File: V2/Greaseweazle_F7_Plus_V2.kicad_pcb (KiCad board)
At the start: 2 copper layers, 80 x 50 mm, 68 parts, among them J1 Wurth 694106301002, J10 PIN1X2, J11 PIN1X2, J12 IDC Box Header, J2 USB_B, J3 Molex 105017-1001, J4 TE EI 171826-4, J5 PIN1X3, J6 PIN1X2, J7 PIN1X5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

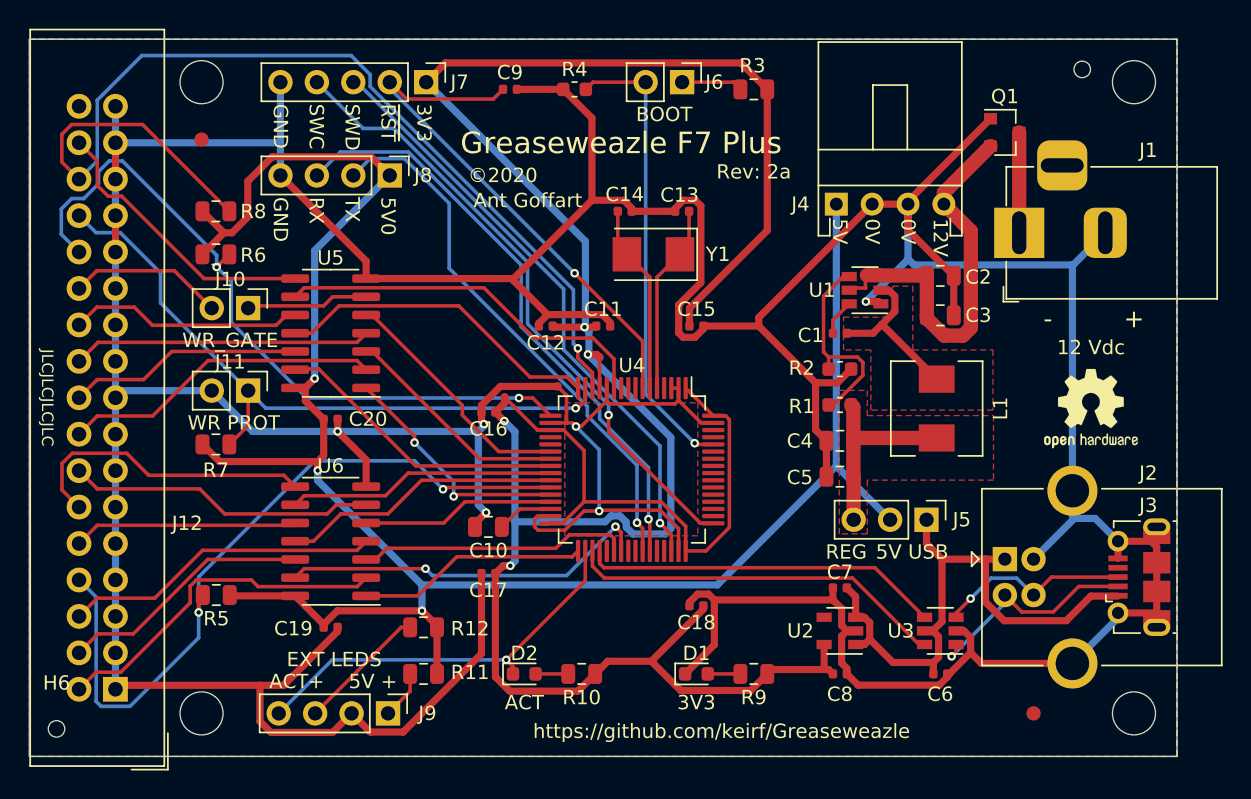
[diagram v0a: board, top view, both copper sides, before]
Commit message: added copper fill below mcu and L1 improved power connections of mcu
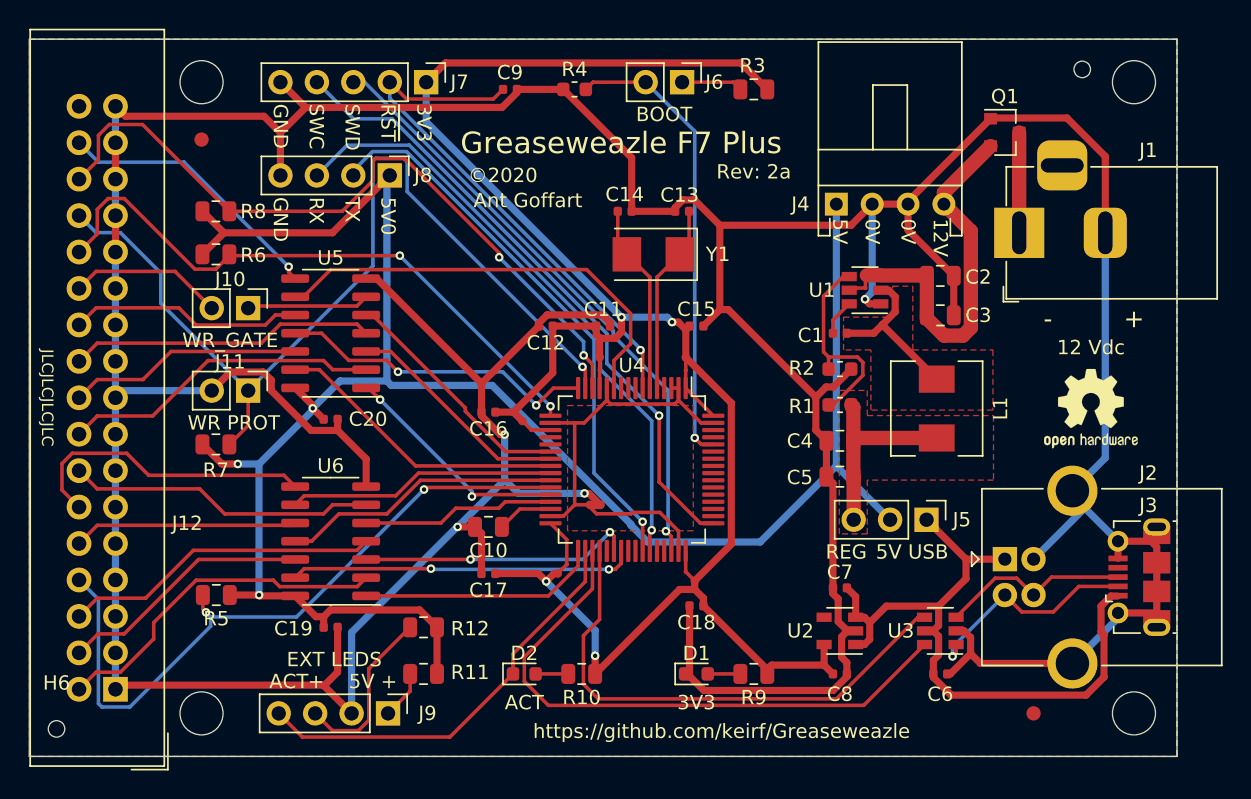
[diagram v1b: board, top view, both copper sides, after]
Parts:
- removed U10: NarrowPowerAdapter, greaseweazle:NarrowPowerAdapter_0.60_to_0.25
- added U11: NarrowPowerAdapter, greaseweazle:NarrowPowerAdapter_0.60_to_0.25, F.Cu at (186.8, 137.2)
- added U12: NarrowPowerAdapter, greaseweazle:NarrowPowerAdapter_0.60_to_0.25, F.Cu at (195.8, 122.2)
- added U13: NarrowPowerAdapter, greaseweazle:NarrowPowerAdapter_0.60_to_0.25, F.Cu at (196.4, 137.8)
- added U15: NarrowPowerAdapter, greaseweazle:NarrowPowerAdapter_0.60_to_0.25_thick, F.Cu at (189.8, 132.5)
- moved U7 3.56 mm to (189.8, 122.2), turned to 0 degrees
- moved U8 2.06 mm to (184.4, 126.6)
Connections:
- U4 pad 1: Net-(U4-Pad1) -> Net-(U12-Pad2)
- U4 pad 12: Net-(U4-Pad12) -> /GND_for_U4
- U4 pad 13: Net-(U10-Pad2) -> Net-(U4-Pad13)
- U4 pad 18: Net-(U4-Pad12) -> /GND_for_U4
- U4 pad 19: Net-(U4-Pad1) -> Net-(U4-Pad19)
- U4 pad 2: Net-(U4-Pad12) -> /GND_for_U4
- U4 pad 3: Net-(U4-Pad12) -> /GND_for_U4
- U4 pad 31: Net-(U4-Pad12) -> /GND_for_U4
- U4 pad 32: Net-(U4-Pad1) -> Net-(U11-Pad2)
- U4 pad 47: Net-(U4-Pad12) -> /GND_for_U4
- U4 pad 48: Net-(U4-Pad1) -> Net-(U13-Pad2)
- U4 pad 63: Net-(U4-Pad12) -> /GND_for_U4
- U4 pad 64: Net-(U4-Pad1) -> Net-(U12-Pad2)
- U7 pad 1: GND -> +3V3
- U7 pad 2: Net-(U4-Pad12) -> Net-(U4-Pad13)
- U8 pad 2: Net-(U4-Pad1) -> Net-(U4-Pad19)
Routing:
- net Net-(U4-Pad12): track 38.3 -> 0.00 mm, vias 2 -> 0
- net Net-(U4-Pad1): track 37.4 -> 0.00 mm
- net /GND_for_U4: track 0.00 -> 32.3 mm
- net +3V3: track 152.7 -> 126.6 mm
- net /~RD_DAT~: track 73.3 -> 51.6 mm, vias 1 -> 2
- net /~WR_PROT~: track 47.5 -> 65.5 mm
- net /USB_D-: track 26.5 -> 41.4 mm
- net /USB_D+: track 25.1 -> 36.3 mm
- net /~TRK_00~: track 50.2 -> 42.9 mm
- net /USB_VBUS: track 41.1 -> 47.2 mm
- net GND: track 381.9 -> 376.8 mm
- net /~SIDE~: track 26.6 -> 31.1 mm
- net Net-(U12-Pad2): track 0.00 -> 3.97 mm
- net Net-(U11-Pad2): track 0.00 -> 3.34 mm
- net /~INDEX~: track 52.6 -> 49.3 mm
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- added copper zone on F.Cu, net /GND_for_U4
- removed copper zone on F.Cu, net Net-(U4-Pad12)

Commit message: added via to get better copper fill made 5Vreg thicker
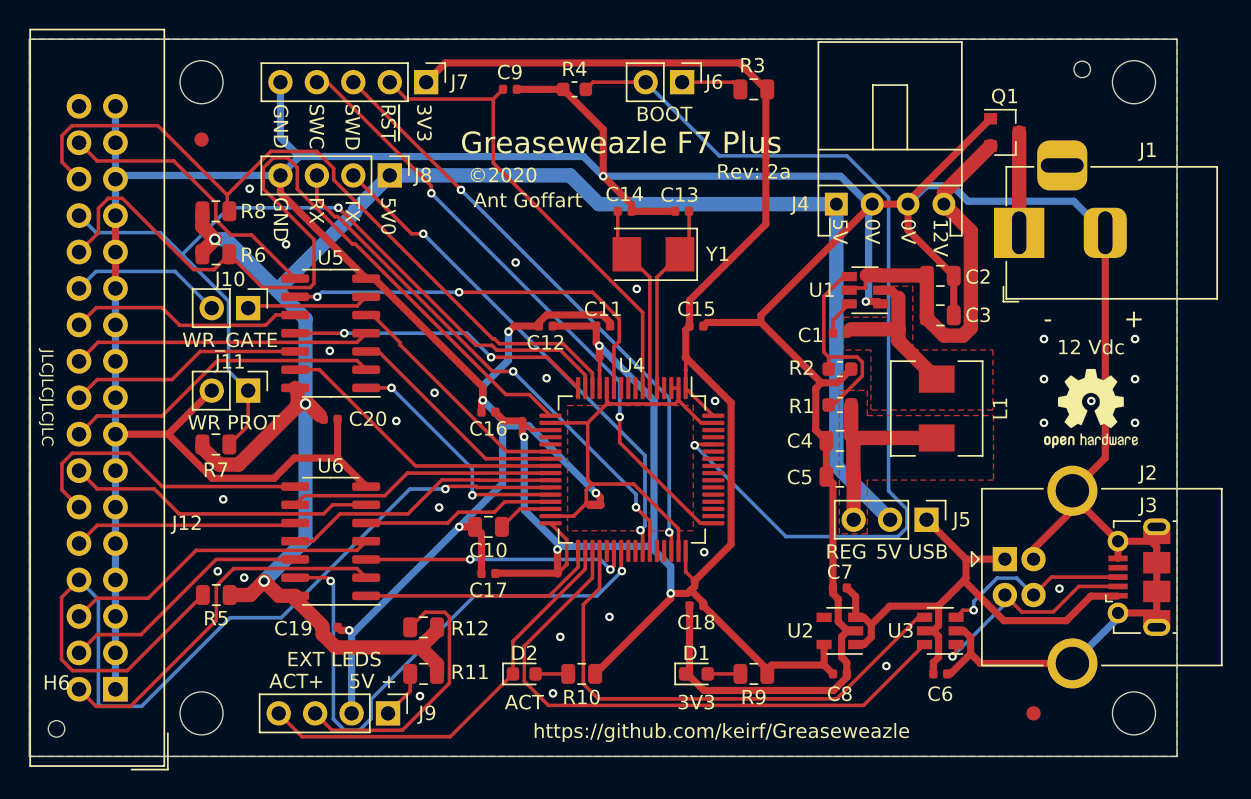
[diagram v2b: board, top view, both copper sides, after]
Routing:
- net /BOOT: track 32.1 -> 67.2 mm
- net /~TRK_00~: track 42.9 -> 60.7 mm, vias 2 -> 0
- net /~INDEX~: track 49.3 -> 65.6 mm, vias 2 -> 1
- net /~PIN4~: track 24.0 -> 39.5 mm
- net GND: track 376.8 -> 389.4 mm, vias 4 -> 34
- net +3V3: track 126.6 -> 137.9 mm
- net +5V: track 141.4 -> 131.6 mm
- net /USB_VBUS: track 47.2 -> 40.1 mm
- net Net-(J9-Pad3): track 12.2 -> 19.1 mm
- net /~WR_PROT~: track 65.5 -> 59.2 mm
- net /RX: track 42.7 -> 36.8 mm, vias 1 -> 2
- net /~RST~: track 37.3 -> 33.1 mm, vias 1 -> 0
- net /TX: track 39.2 -> 35.3 mm, vias 1 -> 2
- net /~SIDE~: track 31.1 -> 28.5 mm, vias 0 -> 2
- net /~PIN2_5V~: track 24.3 -> 26.2 mm
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
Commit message: changed C10 from 10u to 4.7u according to STM doc changed 74LS07 to 74LVC07APW,118 to reduce cost
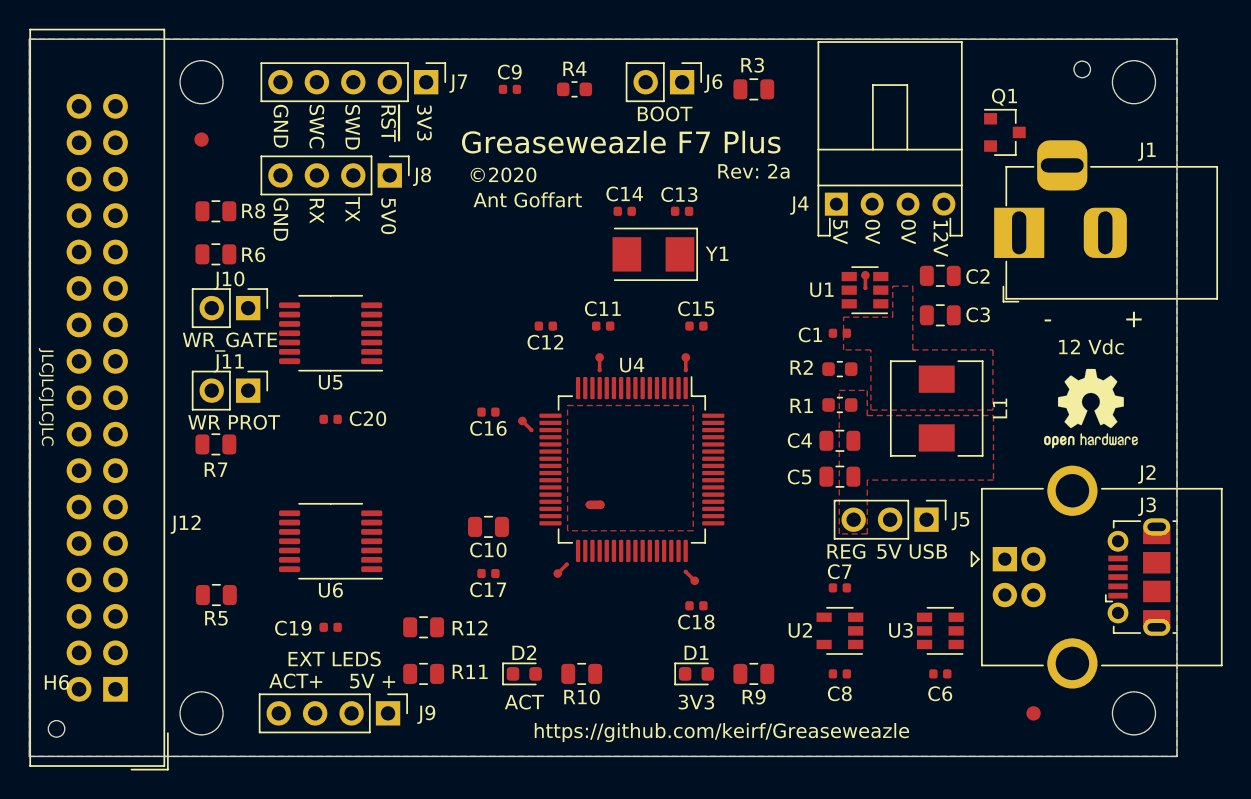
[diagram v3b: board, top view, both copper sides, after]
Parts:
- C10: value 10U -> 4.7uF
- U5, U6: value 74LS07 -> 74LVC07APW,118; footprint Package_SO:SOIC-14_3.9x8.7mm_P1.27mm -> Package_SO:TSSOP-14_4.4x5mm_P0.65mm
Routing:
- net GND: track 389.4 -> 0.00 mm, vias 34 -> 0
- net +3V3: track 137.9 -> 0.00 mm, vias 4 -> 0
- net +5V: track 131.6 -> 0.00 mm, vias 3 -> 0
- net /BOOT: track 67.2 -> 0.00 mm, vias 1 -> 0
- net /~INDEX~: track 65.6 -> 0.00 mm, vias 1 -> 0
- net /~TRK_00~: track 60.7 -> 0.00 mm
- net /~WR_PROT~: track 59.2 -> 0.00 mm, vias 1 -> 0
- net /~RD_DAT~: track 53.2 -> 0.00 mm
- net /SWCLK: track 43.2 -> 0.00 mm, vias 2 -> 0
- net /SWDIO: track 41.9 -> 0.00 mm, vias 2 -> 0
- net /USB_D-: track 41.4 -> 0.00 mm
- net /USB_VBUS: track 40.1 -> 0.00 mm
- net /~PIN4~: track 39.5 -> 0.00 mm, vias 2 -> 0
- net /RX: track 36.8 -> 0.00 mm, vias 2 -> 0
- net /USB_D+: track 36.3 -> 0.00 mm
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
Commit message: routed latest version
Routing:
- net GND: track 0.00 -> 407.7 mm, vias 0 -> 16
- net +5V: track 0.00 -> 143.1 mm, vias 0 -> 5
- net +3V3: track 0.00 -> 136.5 mm, vias 0 -> 4
- net /~WR_PROT~: track 0.00 -> 86.2 mm
- net /~RD_DAT~: track 0.00 -> 50.9 mm
- net /SWCLK: track 0.00 -> 50.2 mm, vias 0 -> 1
- net /SWDIO: track 0.00 -> 42.1 mm, vias 0 -> 1
- net /RX: track 0.00 -> 42.1 mm, vias 0 -> 1
- net /~RST~: track 0.00 -> 41.1 mm, vias 0 -> 1
- net /~TRK_00~: track 0.00 -> 40.5 mm
- net /~INDEX~: track 0.00 -> 39.1 mm
- net /TX: track 0.00 -> 38.6 mm, vias 0 -> 1
- net /USB_VBUS: track 0.00 -> 38.3 mm
- net /USB_D-: track 0.00 -> 35.3 mm
- net /GND_for_U4: track 0.00 -> 34.9 mm
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
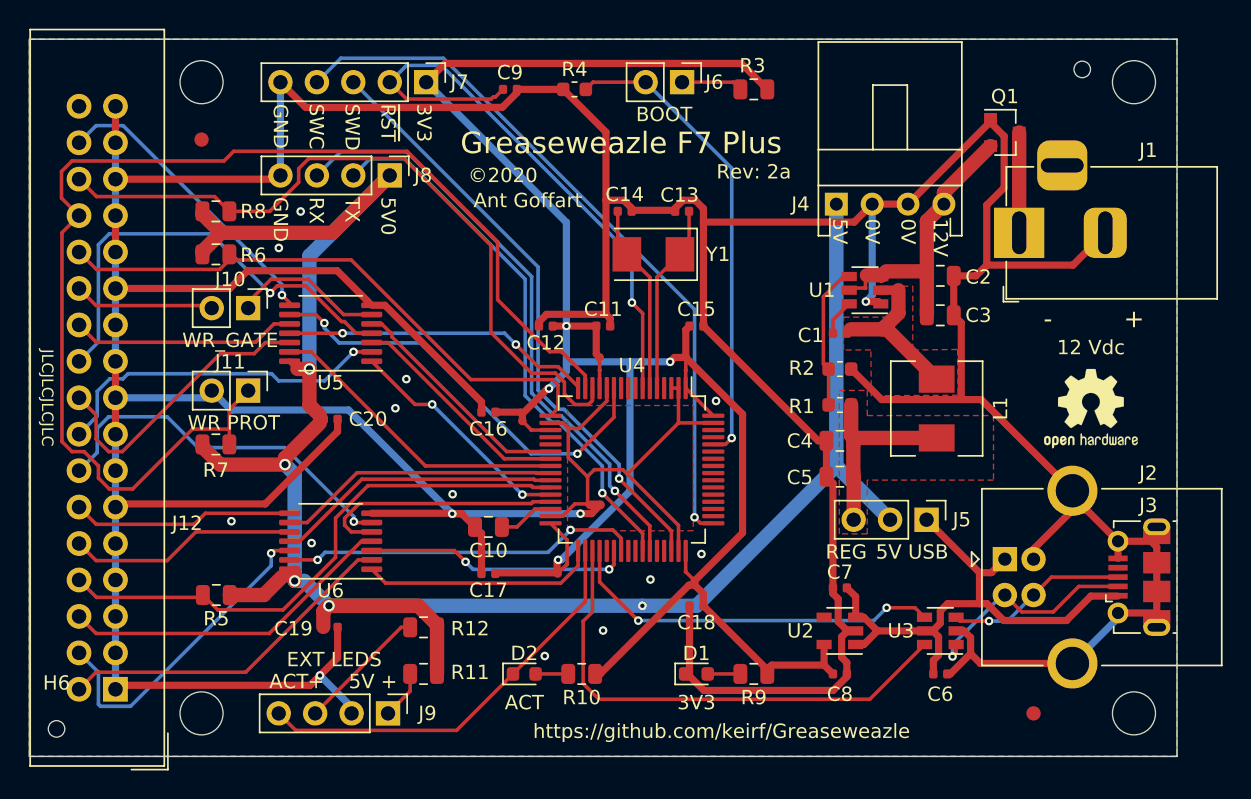
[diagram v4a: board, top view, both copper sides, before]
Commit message: replaced 3.3V regulator by cheaper one moved many parts to make space
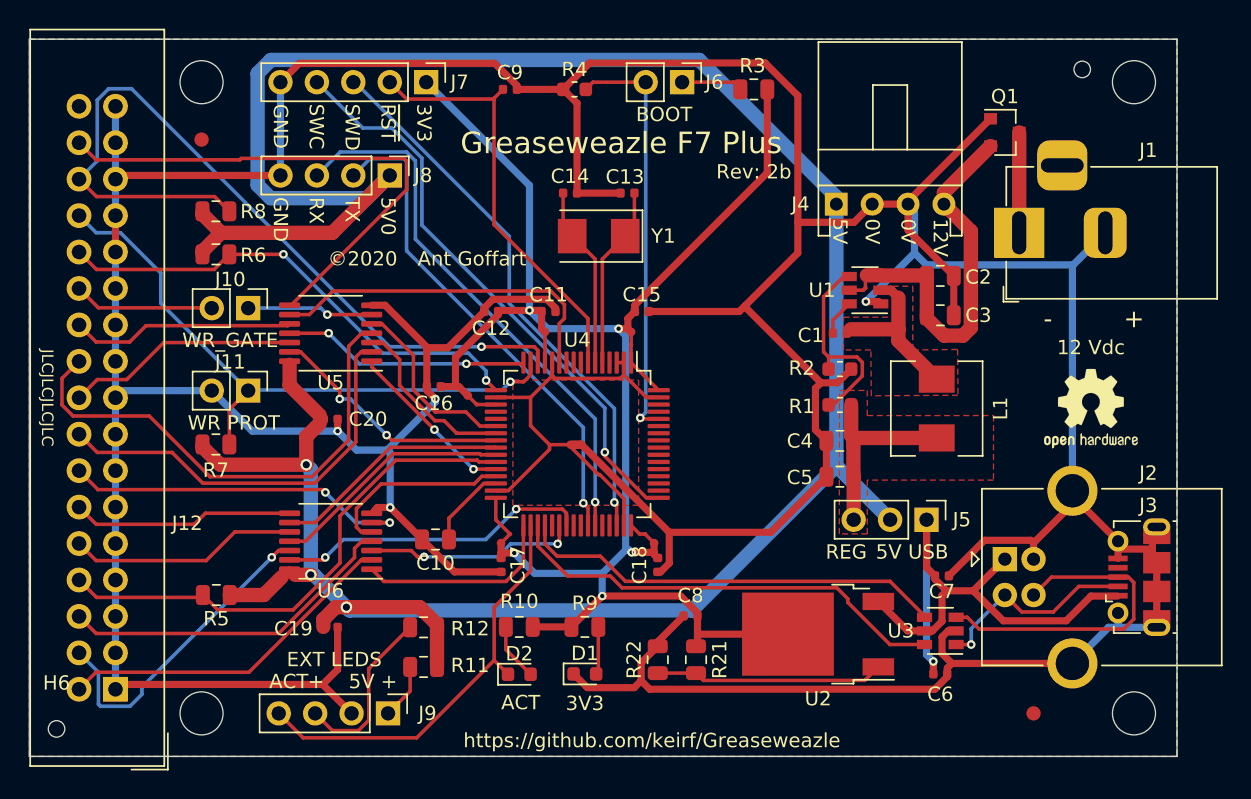
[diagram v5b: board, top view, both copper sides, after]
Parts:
- added R21: 220R, Resistor_SMD:R_0805_2012Metric, F.Cu at (196.5, 143.3)
- added R22: 330R, Resistor_SMD:R_0805_2012Metric, F.Cu at (193.8, 143.3)
- U2: value TLV75533PDBV -> LM317AG-TN3-R; footprint Package_TO_SOT_SMD:SOT-23-5 -> Package_TO_SOT_SMD:TO-252-2
- moved R9 12.2 mm to (188.7, 141.0), turned to 0 degrees
- moved C8 11.2 mm to (196.1, 140.2), turned to 180 degrees
- moved D1 7.78 mm to (188.7, 144.2)
- moved C7 7.16 mm to (213.6, 137.4), turned to 0 degrees
- moved R10 5.45 mm to (184.2, 141.0)
- moved U11 4.48 mm to (182.9, 135.1)
- moved U15 4.40 mm to (188.5, 128.3)
- moved C16 4.20 mm to (178.2, 124.2)
- moved U8 4.20 mm to (180.6, 124.8)
- moved U12 4.20 mm to (191.9, 120.4)
- moved U4 4.20 mm to (188.2, 128.2)
- moved U7 4.20 mm to (185.9, 120.4)
- moved C13 4.02 mm to (191.7, 110.7)
- moved C14 4.02 mm to (187.7, 110.7)
- moved Y1 4.02 mm to (189.7, 113.7)
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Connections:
- U2 pad 1: /USB_VBUS -> Net-(R21-Pad2)
- U2 pad 2: GND -> +3V3
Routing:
- net +5V: track 143.1 -> 189.4 mm, vias 5 -> 3
- net /~WR_PROT~: track 86.2 -> 43.4 mm, vias 0 -> 1
- net +3V3: track 136.5 -> 113.5 mm, vias 4 -> 5
- net /~SIDE_5V~: track 20.9 -> 37.0 mm, vias 1 -> 0
- net Net-(R21-Pad2): track 0.00 -> 16.0 mm
- net /~RST~: track 41.1 -> 29.8 mm, vias 1 -> 0
- net /USB_DIN+: track 12.7 -> 23.2 mm, vias 1 -> 0
- net /SWCLK: track 50.2 -> 40.5 mm
- net +12V: track 18.1 -> 25.9 mm
- net /~TRK_00~: track 40.5 -> 34.3 mm, vias 0 -> 2
- net /~RD_DAT~: track 50.9 -> 56.9 mm, vias 0 -> 1
- net /~SIDE~: track 29.9 -> 24.4 mm, vias 2 -> 0
- net /~M1_5V~: track 24.2 -> 29.1 mm, vias 1 -> 0
- net /~WR_DAT~: track 21.8 -> 17.2 mm
- net /~M1~: track 16.3 -> 12.0 mm
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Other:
- board text added: "Rev: 2b"
- board text removed: "Rev: 2a"

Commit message: added 2nd CMT file to remove 5V regulator to save cost rotated U2 back by 180° added vias to get better copperfill
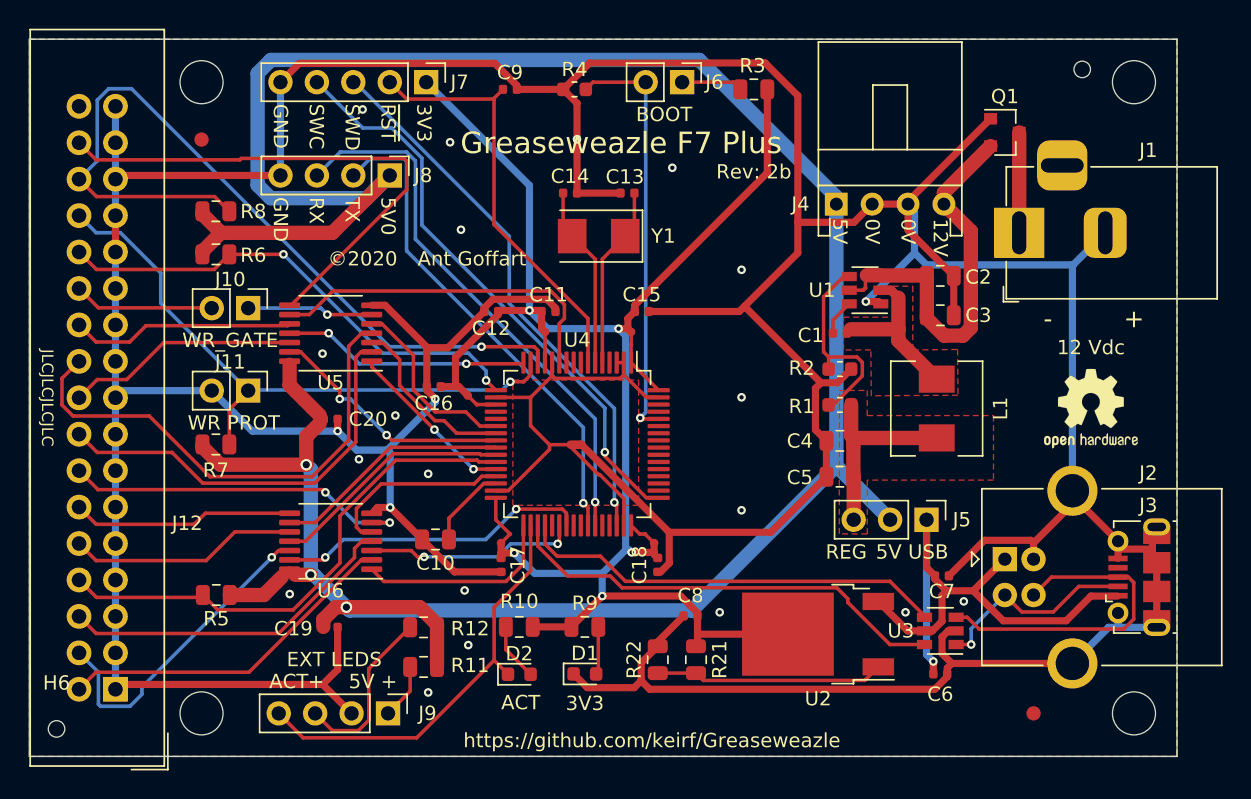
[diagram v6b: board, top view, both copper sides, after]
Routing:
- net GND: vias 4 -> 23
